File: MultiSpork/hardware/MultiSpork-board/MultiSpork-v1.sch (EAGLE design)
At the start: 108 parts, among them U1 USD-SOCKETNEW, U2 SAM3SA-MU, U3 MAX11300GTL, U4 MIC2954, U5 MIC5201-3.3BS, U7 MCP73831

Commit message: Updated board with: 	-- Voltage regulators 	-- CC3100 WiFi
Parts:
- added C37, C40, C41, C42, C45, C46, C48, C51, C52, C54, C57, C58, C60, C61, C62: (no value), resistor:C-EUC1210
- added C38, C39, C43, C44, C47, C49, C50, C53, C55, C56, C59: (no value), resistor:C-EUC0603
- added C63, C67, C69, C70, C71, C73, C74, C75, C76, C77, C80: 100n, resistor:C-EUC0603
- added C64, C65, C66: 4u7, resistor:C-EUC0603
- added C68, C72: 10u, resistor:C-EUC0603
- added C78, C79: 22u, resistor:C-EUC1206
- added D15, D16, D17, D18, D19: (no value), diode:DIODE-SMB
- added JP2: (no value), pinhead:PINHD-1X6
- added JP3: (no value), pinhead:PINHD-1X4
- added L10, L12: 2u2, SparkFun-Passives:INDUCTOR1206H*
- added L11: 1u, SparkFun-Passives:INDUCTOR1206H*
- added L3, L4, L5, L6, L7, L8, L9: NR6028, logos-inductors:NR6028
- added R1, R14, R15, R16, R17, R18, R19, R20, R21, R22, R23, R24: (no value), resistor:R-EU_R0603
- added R25, R32: 10K, resistor:R-EU_R0603
- added R26, R27, R28, R31, R33, R34, R35: 100K, resistor:R-EU_R0603
- added R29, R30: 4K7, resistor:R-EU_R0603
- added U6, U8: LT3580EMS8E, MultiSpork-parts:LT3580EMS8E
- added U9: CC3100, CC3100:CC3100
- D14: PARTNO B150B-13-F -> LSM115JE3
- F2: value 500 mA -> 1500 mA
- U4: value MIC2954 -> LT3580EMS8E; device logos-power:MIC2954 -> MultiSpork-parts:LT3580EMS8E
- U5: value MIC5201-3.3BS -> LT3580EMS8E; device logos-power:MIC5201-3.3BS -> MultiSpork-parts:LT3580EMS8E
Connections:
- removed net RXD: R6B.2
- removed net TXD: R6C.2
- new net CC_CS: U2G$5.PA0/PGMEN0, U9G$5.HOST_SPI_CS
- new net CC_INT: R25.2, U2G$5.PA2/PGMEN2, U9G$5.HOST_INTR
- new net CC_NHIB: R28.1, U2G$5.PA1/PGMEN1, U9G$5.NHIB
- new net CC_RST: C80.1, JP2.5, R27.1, U2G$5.PA7/XIN32/PGMNVALID, U9G$5.NRESET
- new net N$100: JP3.3, U9G$6.TEST_59
- new net N$101: JP3.4, U9G$6.TEST_58
- new net N$102: R35.2, U9G$1.RSV@0
- new net N$106: JP2.1, U9G$5.UART1_NRTS
- new net N$107: JP2.2, U9G$5.UART1_TX
- new net N$108: JP2.3, U9G$5.UART1_RX
- new net N$109: JP2.4, U9G$5.UART1_NCTS
- new net N$18: C38.1, U4.SS
- new net N$20: R1.2, U4.RT
- new net N$21: R14.1, U4.FB
- new net N$22: R15.1, U4.VC
- new net N$23: C39.1, R15.2
- new net N$24: C43.1, U5.SS
- new net N$25: D16.A, L3.2, U4.SW
- new net N$26: R16.2, U5.RT
- new net N$28: R17.1, U5.FB
- new net N$60: C47.1, R18.1, U5.VC
- new net N$61: C44.1, R18.2
- new net N$63: C45.1, L4.2, U5.SW
- new net N$64: C45.2, D17.A, L5.1
- new net N$65: C55.1, U8.SS
- new net N$66: R22.2, U8.RT
- new net N$67: R23.1, U8.FB
- new net N$68: C49.1, U6.SS
- new net N$69: R19.2, U6.RT
- new net N$70: R20.1, U6.FB
- new net N$71: C53.1, R21.1, U6.VC
- new net N$72: C50.1, R21.2
- new net N$73: C51.1, L6.2, U6.SW
- new net N$74: C51.2, D18.A, L7.1
- new net N$75: C59.1, R24.1, U8.VC
- new net N$76: C56.1, R24.2
- new net N$77: C58.1, L8.2, U8.SW
- new net N$78: C58.2, D19.A, L9.1
- new net N$79: C63.1, U9G$2.VIN_IO2
- new net N$80: C64.1, U9G$2.VIN_DCDC_DIG
- new net N$81: C66.1, U9G$2.VIN_DCDC_ANA
- new net N$82: C67.1, C68.1, C69.1, C70.1, C71.1, L10.1, U9G$2.LDO_IN1, U9G$2.LDO_IN2, U9G$2.VDD_ANA1, U9G$2.VIN_IO1
- new net N$83: C65.1, U9G$2.VIN_DCDC_PA
- new net N$84: L10.2, U9G$2.DCDC_ANA_SW
- new net N$85: C77.1, C78.1, C79.1, U9G$2.DCDC_PA_OUT, U9G$2.VDD_PA_IN
- new net N$87: L11.1, U9G$2.DCDC_PA_SW_P
- new net N$88: L11.2, U9G$2.DCC_PA_SW_N
- new net N$89: L12.2, U9G$2.DCDC_DIG_SW
- new net N$90: C72.1, C73.1, C74.1, L12.1, U9G$2.VDD_DIG1, U9G$2.VDD_DIG2
- new net N$91: R31.2, U9G$6.FORCE_AP
- new net N$92: C75.1, U9G$2.VDD_RAM
- new net N$93: C76.1, U9G$2.VDD_PLL
- new net N$94: R32.2, U9G$6.SOP2/TCXO_EN
- new net N$95: R33.2, U9G$6.SOP1
- new net N$96: R34.2, U9G$6.SOP0
- new net N$98: JP3.1, U9G$6.TEST_62
- new net N$99: JP3.2, U9G$6.TEST_60
- new net RXD0: R6B.2, U2G$5.PA5/PGMRDY
- new net TXD0: R6C.2, U2G$5.PA6/PGMNOE
- net +10V: now also C40.1, C41.1, D16.C, R14.2
- net +3V3: now also C52.1, C62.1, D18.C, R20.2, R27.2, R28.2, R29.2, R30.2, U9G$2.VDD_ANA2; no longer U5.OUT
- net +5V: now also C46.1, C61.1, D17.C, R17.2; no longer U4.OUT
- net +UB: now also D15.A
- net -10V: now also C57.2, C60.2, L9.2, R23.2
- net ACC_CS: now also U2G$5.PA10/PGMM2
- net GND: now also C37.2, C38.2, C39.2, C40.2, C41.2, C42.2, C43.2, C44.2, C46.2, C47.2, C48.2, C49.2, C50.2, C52.2, C53.2, C54.2, C55.2, C56.2, C57.1, C59.2, C60.1, C61.2, C62.2, C63.2, C64.2, C65.2, C66.2, C67.2, C68.2, C69.2, C70.2, C71.2, C72.2, C73.2, C74.2, C75.2, C76.2, C77.2, C78.2, C79.2, C80.2, D19.C, JP2.6, L5.2, L7.2, R1.1, R16.1, R19.1, R22.1, R25.1, R26.1, R31.1, R32.1, R33.1, R34.1, R35.1, U4.GND, U4.SYNC, U5.GND, U5.SYNC, U6.GND, U6.SYNC, U8.GND, U8.SYNC, U9G$2.GND
- net MAX_CS: now also U2G$5.PA11/PGMM3
- net MAX_CVNT: now also U2G$5.PA8/XOUT32/PGMM0
- net MAX_INT: now also U2G$5.PA15/PGMD3
- net MISO: now also R26.2, U2G$5.PA12/PGMD0, U9G$5.HOST_SPI_MISO
- net MOSI: now also U2G$5.PA13/PGMD1, U9G$5.HOST_SPI_MOSI
- net SCL: now also R30.1, U2G$5.PA4/PGMNCMD
- net SCLK: now also U2G$5.PA14/PGMD2, U9G$5.HOST_SPI_CLK
- net SDA: now also R29.1, U2G$5.PA3
- net SD_CS: now also U2G$5.PA9/PGMM1
- net V+: now also C37.1, C42.1, C48.1, C54.1, D15.C, L3.1, L4.1, L6.1, L8.1, U4.!SHDN!, U4.VIN, U5.!SHDN!, U5.VIN, U6.!SHDN!, U6.VIN, U8.!SHDN!, U8.VIN

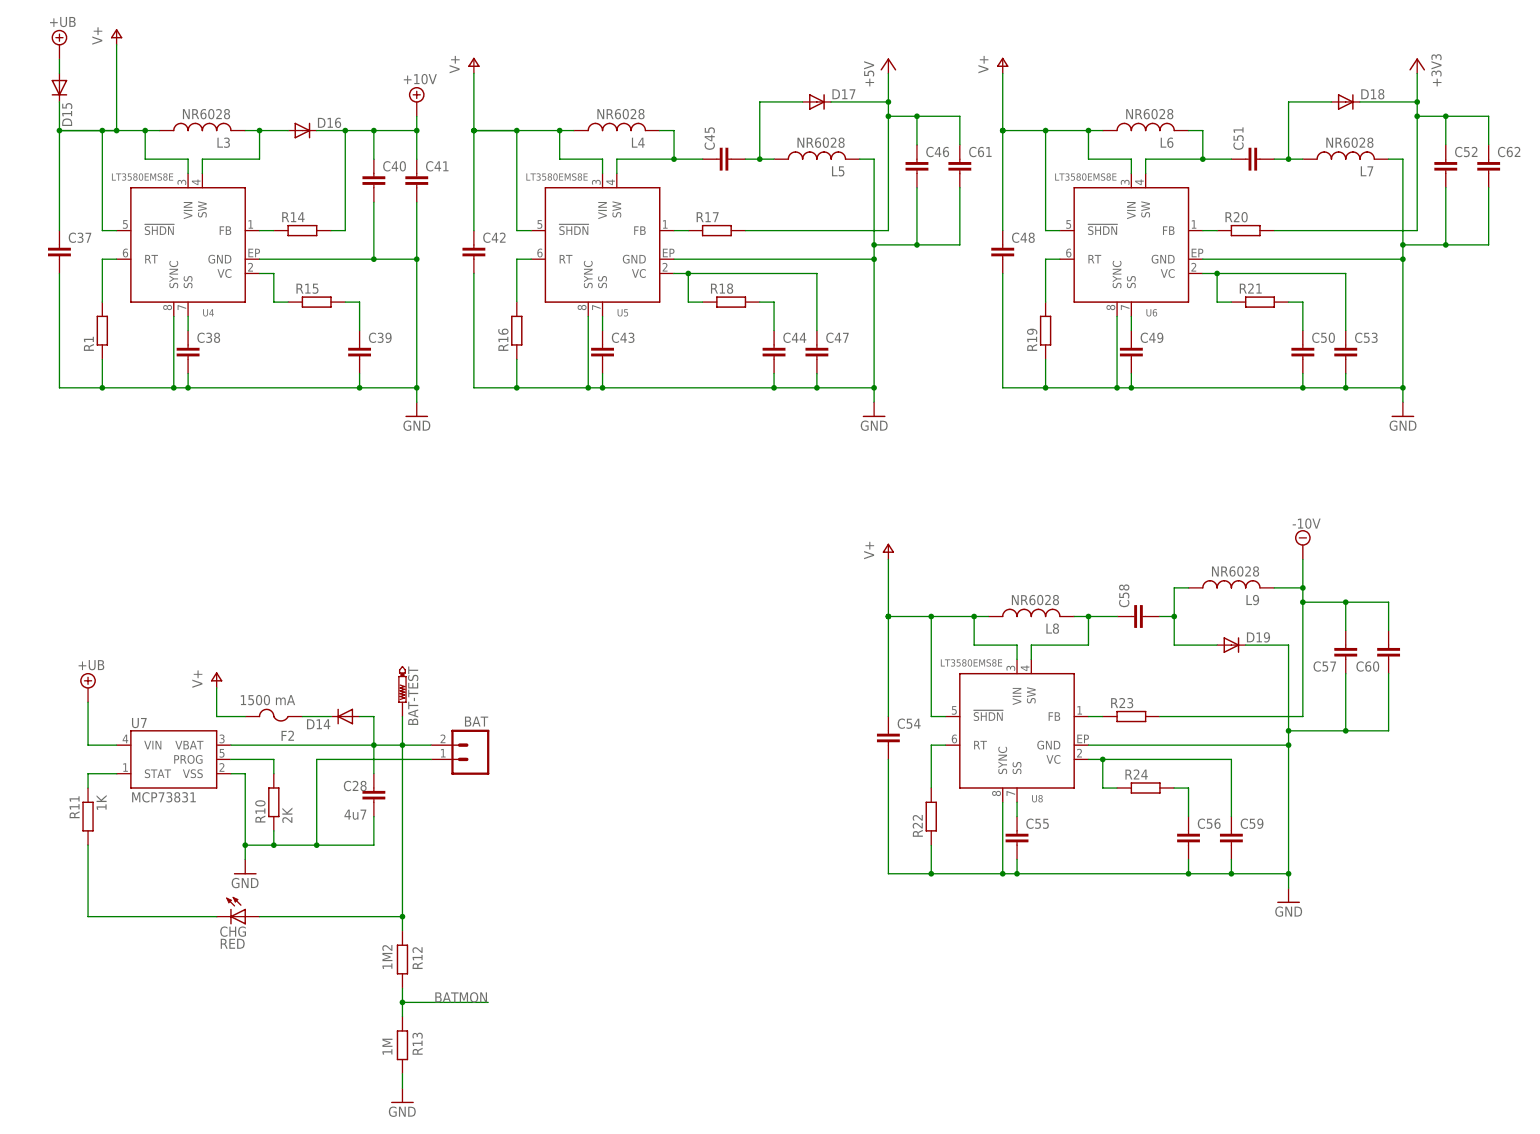
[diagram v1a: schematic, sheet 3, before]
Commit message: -- Added flash chip to CC3100.lbr -- Added 2.4 GHz filter to CC3100.lbr -- Added RF components on schematic -- Added CC3100 crystals on schematic -- Added MAX11300 external temperature sensors -- Fixed some issues with the protection circuitry hookup
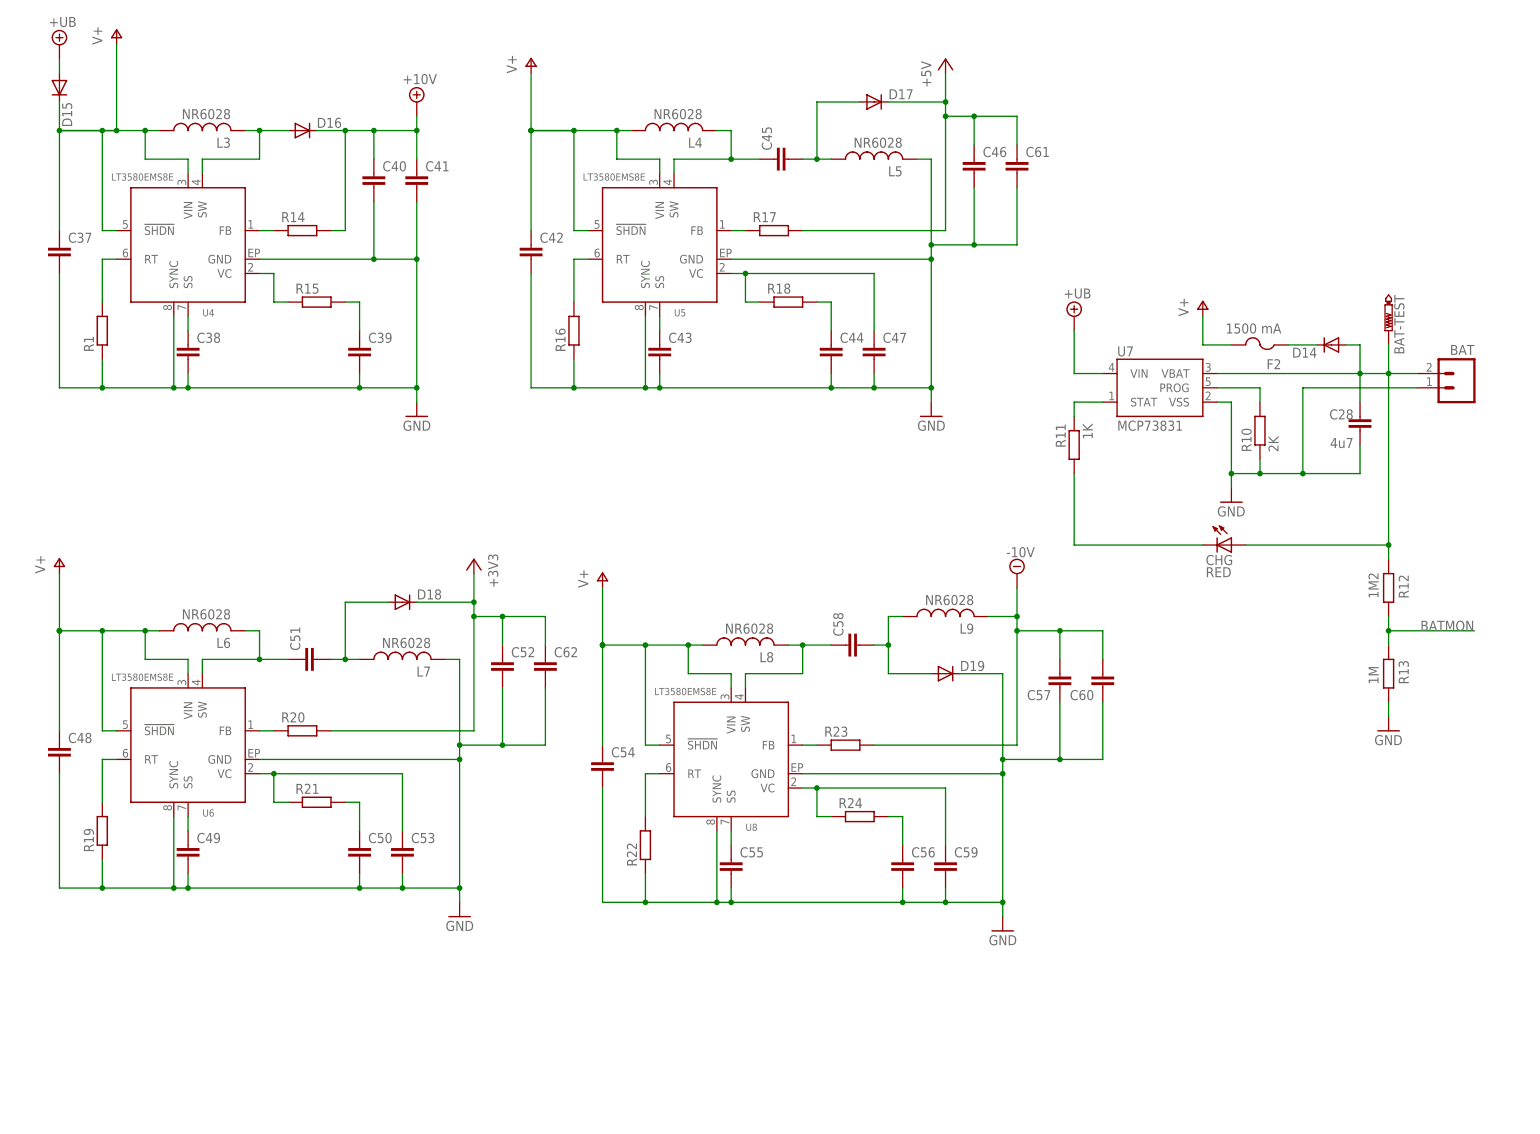
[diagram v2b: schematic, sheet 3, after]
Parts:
- added C81, C82, C83, C84: (no value), resistor:C-EUC0603
- added C85: 100n, resistor:C-EUC0603
- added C86, C87: 100u, resistor:CPOL-EUCT6032
- added FL1: DEA202450BT, CC3100:DEA202450BT
- added Q2: 40 MHz, logos-crystals:ECS-.327-7-34B-TR
- added Q3: 32.768 kHz, logos-crystals:CRYSTALCSM-3X
- added Q4, Q5: MMBT3904, SparkFun-DiscreteSemi:TRANSISTOR_NPNMMBT5088
- added R36: (no value), resistor:R-EU_R0603
- added R37, R38, R39: 100K, resistor:R-EU_R0603
- added RESET: SKHMPSE010, switch:SKHMPSE010
- added U$1: ATMEGA128RFA1_MOLEX-ANT, CC3100:ATMEGA128RFA1_MOLEX-ANT
- added U10: M25PX80, CC3100:M25PX80
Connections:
- new net N$103: C81.1, Q2.1, U9G$3.WLAN_XTAL_N
- new net N$104: C82.1, Q2.2, U9G$3.WLAN_XTAL_P
- new net N$105: C83.1, Q3.1, U9G$3.RTC_XTAL_N
- new net N$110: C84.1, Q3.2, U9G$3.RTC_XTAL_P
- new net N$111: U10.DO, U9G$4.FLASH_SPI_MISO
- new net N$112: R39.1, U10.!CS!, U9G$4.FLASH_SPI_CS
- new net N$113: FL1.IN, U9G$3.RF_BG
- new net N$114: FL1.OUT, U$1.A
- new net N$115: Q5.B, Q5.C, U3-TEMP.D1P
- new net N$116: Q5.E, U3-TEMP.D1N
- new net N$117: Q4.E, U3-TEMP.D0N
- new net N$118: Q4.B, Q4.C, U3-TEMP.D0P
- new net N$86: R38.2, U10.CLK, U9G$4.FLASH_SPI_CLK
- new net N$97: R37.2, U10.DI, U9G$4.FLASH_SPI_MOSI
- net +3V3: now also C29.1, C30.1, C85.1, C86.+, C87.+, R36.2, R39.2, U10.!RST!, U10.!WP!, U10.VCC, U3-PWR.DVDD
- net +5V: no longer C29.1, C30.1, U3-PWR.DVDD
- net GND: now also C81.2, C82.2, C83.2, C84.2, C85.2, C86.-, C87.-, FL1.GND1, FL1.GND2, R37.1, R38.1, RESET.1.1, RESET.1.2, RESET.SH, U10.GND
- net MASTER_RESET: now also R36.1, RESET.2.1, RESET.2.2
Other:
- moved on the sheet: BAT, BAT-TEST, C21, C27, C28, C42, C43, C44, C45, C46, C47, C48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

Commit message: Finished schematic & placement for the prototype
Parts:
- removed U$1: ATMEGA128RFA1_MOLEX-ANT, CC3100:ATMEGA128RFA1_MOLEX-ANT
- added J1: U.FL, SparkFun-Connectors:U.FL
- added R40: (no value), resistor:R-EU_R1206
- ANALOG: value (none) -> 76385-316LF; device pinhead-1:PINHD-2X16_2.54-SMD-90° -> logos-headers:76385-316LF
- C10, C11, C21, C27, C29, C30, C31, C32, C33, C34: device resistor:C-EUC1206 -> resistor:C-EUC0603
- D16, D18, D19: device diode:DIODE-SMB -> adafruit:DIODESMA
- D17: device diode:DIODE-SMB -> adafruit:DIODESOD-123
- L3, L8: value NR6028 -> L-US2323; device logos-inductors:NR6028 -> logos-inductors:L-US2323
- L4, L5, L6, L7, L9: value NR6028 -> L-US1008; device logos-inductors:NR6028 -> logos-inductors:L-US1008
- Q2: value 40 MHz -> 32.768 kHz
- Q3: value 32.768 kHz -> 40 MHz
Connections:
- removed net N$56 (its old number): F7.2, F8.2, F9.2
- removed net N$59: F10.2, F11.2, F12.2, F13.2
- removed net N$62: F14.2, F15.2, F16.2
- removed net PORT0: F3.2
- removed net PORT1: F4.2
- removed net PORT2: F5.2
- removed net PORT3: F6.2
- net ACC_CS: now also R6B.2; no longer R7D.1
- net AGND: now also R40.1
- net GND: now also J1.GND@0, J1.GND@1, R40.2
- net MISO: now also R2A.2, R6D.2; no longer R2D.2, R7C.1
- net MOSI: now also R2C.2; no longer R2B.2
- net N$10: now also R7C.2; no longer R7B.2
- net N$103: now also Q3.1; no longer Q2.1
- net N$104: now also Q3.2; no longer Q2.2
- net N$105: now also Q2.1; no longer Q3.1
- net N$11: now also R6D.1; no longer R7C.2
- net N$110: now also Q2.2; no longer Q3.2
- net N$114: now also J1.SIGNAL; no longer U$1.A
- net N$12: now also R6B.1; no longer R7D.2
- net N$13: now also R6A.1; no longer R6A.2
- net N$14: now also R7D.2; no longer R6C.1
- net N$15: now also R7B.2; no longer R6B.1
- net N$16: now also R6C.1; no longer R6D.1
- net N$2: now also R2D.1; no longer R2A.1
- net N$4: now also R2C.1; no longer R2B.1
- net N$5: now also R2B.1; no longer R2C.1
- net N$6: now also R2A.1; no longer R2D.1
- net PORT00: now also F3.2
- net PORT01: now also F4.2
- net PORT02: now also F5.2
- net PORT03: now also F6.2
- net PORT04: now also F7.2
- net PORT05: now also F8.2
- net PORT06: now also F9.2
- net PORT07: now also F10.2
- net PORT08: now also F11.2
- net PORT09: now also F12.2
- net PORT10: now also F13.2
- net PORT11: now also F14.2
- net PORT12: now also F15.2
- net PORT13: now also F16.2
- net RXD0: now also R7B.1; no longer R6B.2
- net SCL: now also R6C.2; no longer R6D.2
- net SCLK: now also R2B.2, R7C.1; no longer R2C.2, R7B.1
- net SDA: now also R6A.2; no longer R6A.1
- net SD_CS: now also R2D.2; no longer R2A.2
- net TXD0: now also R7D.1; no longer R6C.2
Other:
- moved on the sheet: Q2, Q3, R2A, R2B, R2C, R2D, R6A, R6B, R6C, R6D, R7B, R7C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
